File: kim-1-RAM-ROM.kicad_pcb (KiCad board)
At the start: 2 copper layers, 113.5 x 134.6 mm, 42 parts, among them J1 Conn_03x08, J2 Conn_03x06, J3 Conn_02x08_Counter_Clockwise, SW1 Vectors, SW2 SW_DIP_x08, SW3 SW_DIP_x07, SW4 SW_DIP_x01, SW5 SW_DIP_x01, SW6 Image_set, U1 74LS04, U10 SST39SF020, U11 628128, U2 74LS08, U3 74LS08, U4 74HCT541, U5 74HCT541, U6 74LS133, U7 74LS145, U8 74LS145, U9 74LS145, X1 EDGE_CONN

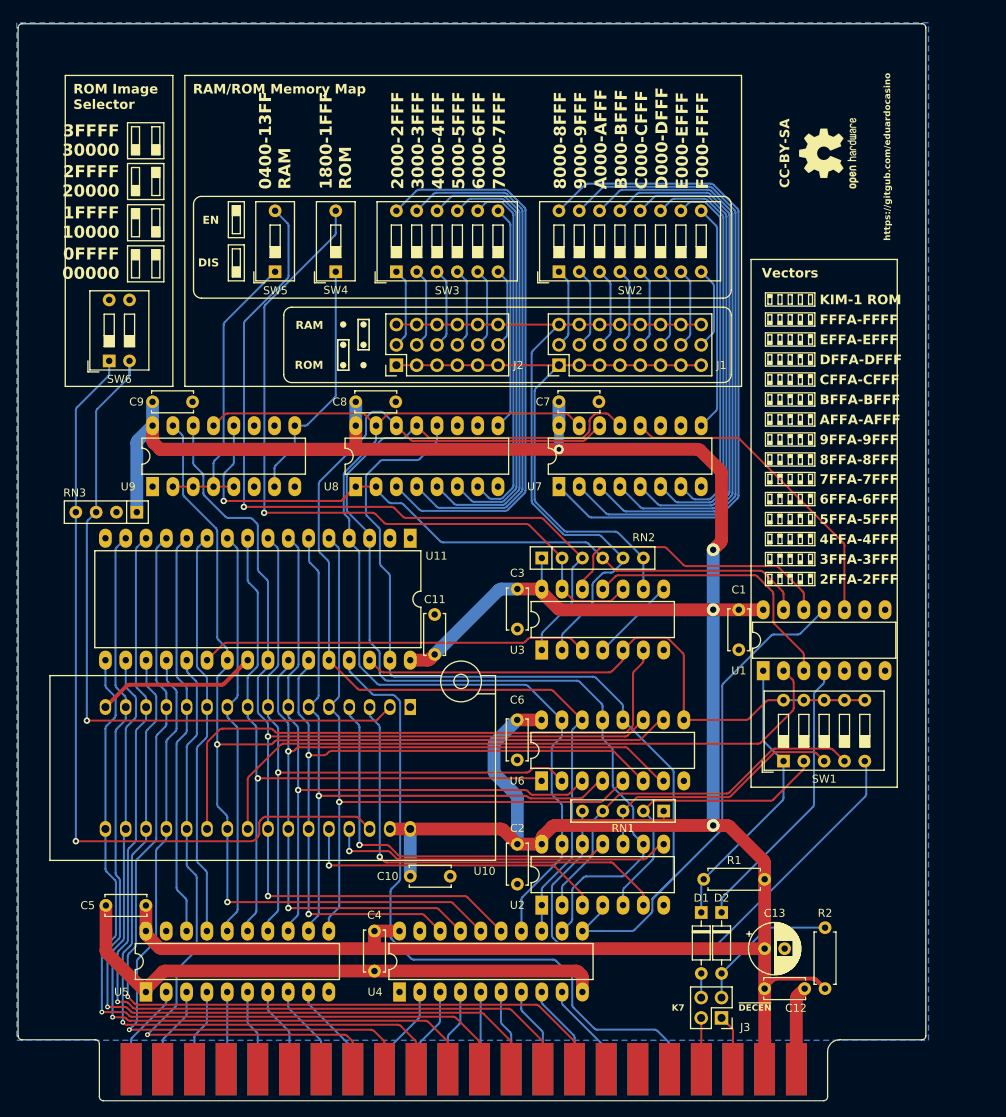
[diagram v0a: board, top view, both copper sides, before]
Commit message: Add option to support the MTU floppy controller boot prom
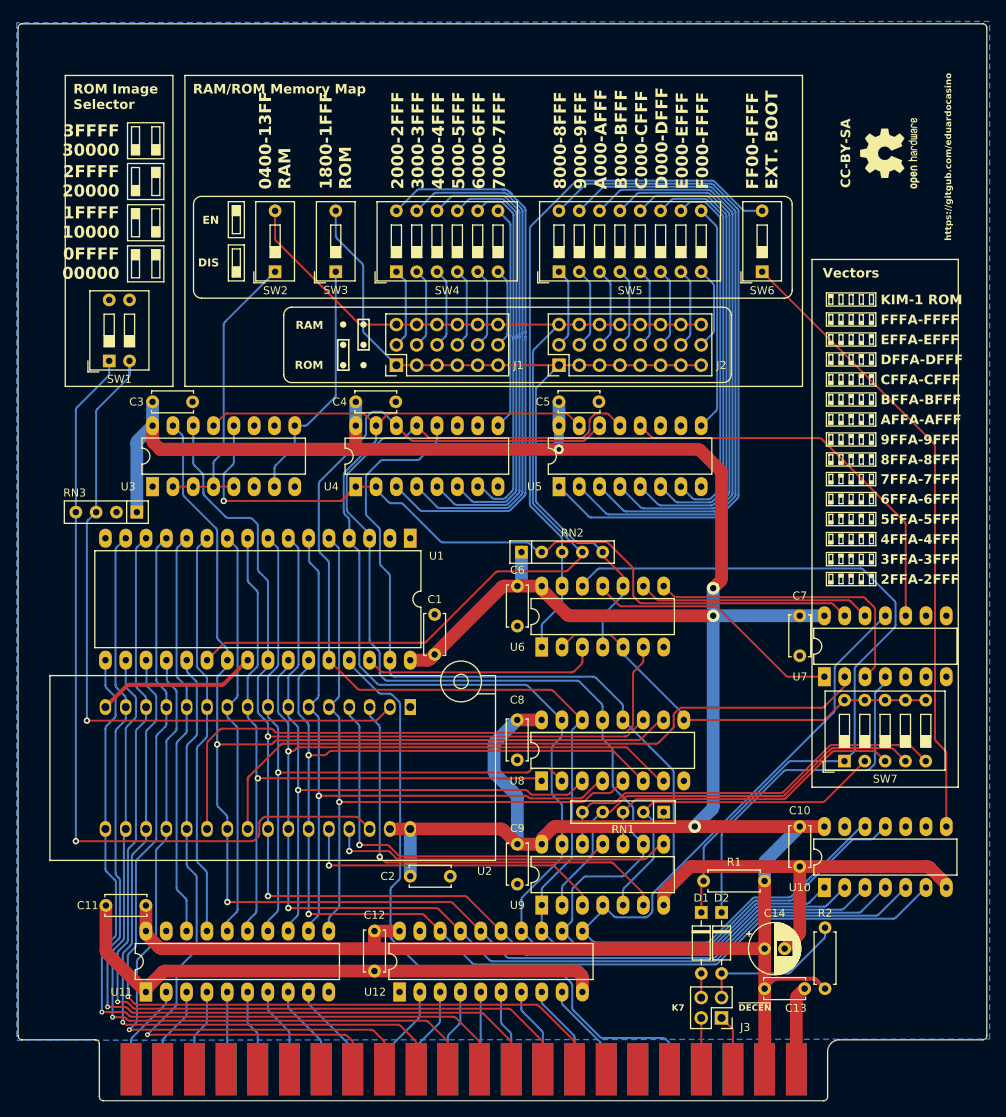
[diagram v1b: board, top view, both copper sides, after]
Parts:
- added C10: 100nF, Capacitor_THT:C_Disc_D5.0mm_W2.5mm_P5.00mm, F.Cu at (149.5, 167.1)
- added SW6: SW_DIP_x01, Button_Switch_THT:SW_DIP_SPSTx01_Slide_9.78x4.72mm_W7.62mm_P2.54mm, F.Cu at (144.8, 97.8)
- added U10: 74LS30, Package_DIP:DIP-14_W7.62mm_LongPads, F.Cu at (152.6, 174.8)
- RN2: footprint Resistor_THT:R_Array_SIP6 -> Resistor_THT:R_Array_SIP5
- moved U7 7.69 mm to (152.6, 148.4)
- moved C7 7.66 mm to (149.5, 140.8)
- moved REF** 7.62 mm to (160.7, 83.0)
- moved SW7 7.62 mm to (155.1, 158.9)
- moved RN2 2.65 mm to (114.7, 132.8)
- moved C6 0.37 mm to (114.2, 137.1)
- moved U6 0.37 mm to (117.2, 144.7)
- moved R1 0.21 mm to (137.4, 173.9)
- moved RN1 0.13 mm to (132.5, 165.3)
- renumbered C11 to C1, C5 to C11, C4 to C12, C12 to C13, C13 to C14, C10 to C2, C9 to C3, C8 to C4, C7 to C5, C3 to C6, C1 to C7, C6 to C8, C2 to C9, J2 to J1, J1 to J2, SW6 to SW1, SW5 to SW2, SW4 to SW3, SW3 to SW4, SW2 to SW5, SW1 to SW7, U11 to U1, U5 to U11, U4 to U12, U10 to U2, U9 to U3, U8 to U4, U7 to U5, U3 to U6, U1 to U7, U6 to U8, U2 to U9
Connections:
- RN2 pad 4: Net-(RN2-R3) -> Net-(J1-Pin_12)
- RN2 pad 5: Net-(J1-Pin_12) -> Net-(J1-Pin_1)
- SW2 pad 2: Net-(RN2-R2) -> Net-(J1-Pin_12)
- SW3 pad 2: Net-(RN2-R1) -> Net-(J1-Pin_1)
- SW7 pad 10: Net-(U11-CS2) -> Net-(SW7-Pad10)
- SW7 pad 6: Net-(U11-CS2) -> Net-(SW7-Pad10)
- SW7 pad 7: Net-(U11-CS2) -> Net-(SW7-Pad10)
- SW7 pad 8: Net-(U11-CS2) -> Net-(SW7-Pad10)
- SW7 pad 9: Net-(U11-CS2) -> Net-(SW7-Pad10)
- U1 pad 22: Net-(U11-~{CS1}) -> Net-(J1-Pin_12)
- U1 pad 30: Net-(U11-CS2) -> Net-(U1-CS2)
- U3 pad 12: Net-(RN2-R3) -> Net-(RN2-R1)
- U4 pad 1: Net-(RN2-R3) -> Net-(RN2-R1)
- U4 pad 2: Net-(RN2-R3) -> Net-(RN2-R1)
- U6 pad 10: Net-(RN2-R1) -> Net-(J1-Pin_1)
- U6 pad 11: Net-(U1-Pad3) -> Net-(U6-Pad11)
- U6 pad 12: Net-(U1-Pad12) -> Net-(D1-K)
- U6 pad 13: Net-(RN2-R1) -> Net-(RN2-R2)
- U6 pad 2: Net-(J1-Pin_12) -> Net-(SW7-Pad10)
- U6 pad 3: Net-(U11-~{CS1}) -> Net-(U1-CS2)
- U6 pad 4: Net-(U3-Pad4) -> Net-(J1-Pin_1)
- U6 pad 5: Net-(U11-CS2) -> Net-(SW7-Pad10)
- U6 pad 8: Net-(U3-Pad4) -> Net-(U6-Pad8)
- U6 pad 9: Net-(J1-Pin_1) -> Net-(U6-Pad9)
- U7 pad 1: Net-(D1-K) -> Net-(U6-Pad11)
- U7 pad 12: Net-(U1-Pad12) -> Net-(U6-Pad9)
- U7 pad 13: Net-(RN2-R3) -> Net-(RN2-R1)
- U7 pad 3: Net-(U1-Pad3) -> Net-(U6-Pad8)
- U8 pad 9: Net-(U11-CS2) -> Net-(SW7-Pad10)
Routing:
- net Net-(RN2-R3): track 90.8 -> 0.00 mm, vias 1 -> 0
- net Net-(SW6-Pad1): track 0.00 -> 78.8 mm
- net Net-(U11-CS2): track 75.0 -> 0.00 mm
- net /A8: track 93.7 -> 160.1 mm
- net /A9: track 103.6 -> 164.6 mm
- net Net-(D1-K): track 35.8 -> 94.9 mm
- net /A10: track 153.3 -> 208.9 mm
- net Net-(J1-Pin_12): track 91.2 -> 146.3 mm
- net Net-(SW7-Pad10): track 0.00 -> 52.3 mm
- net GND: track 101.5 -> 152.0 mm
- net /A11: track 143.9 -> 194.0 mm
- net Net-(U11-~{CS1}): track 48.6 -> 0.00 mm
- net /A14: track 133.0 -> 180.2 mm
- net /A12: track 138.0 -> 182.7 mm
- net /A13: track 128.0 -> 167.3 mm
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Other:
- board size 113.5 x 134.6 mm -> 121.1 x 134.6 mm
- board text added: "FF00-FFFF EXT. BOOT"

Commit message: Minor silkscreen changes
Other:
- board text added: "1"
- board text added: "22"
- board text added: "A"
- board text added: "Z"
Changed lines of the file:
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@@
   (gr_line (start 154.45 193.78) (end 172.35 193.78)
     (stroke (width 0.1) (type default)) (layer "Edge.Cuts"))
+  (gr_text "Z" (at 151.04 193.3) (layer "B.SilkS")
+    (effects (font (size 1 1) (thickness 0.15)) (justify right bottom mirror))
+  )
+  (gr_text "A" (at 63.88 193.3) (layer "B.SilkS")
+    (effects (font (size 1 1) (thickness 0.15)) (justify left bottom mirror))
+  )
   (gr_text "F000-FFFF" (at 138.19 87.48 90) (layer "F.SilkS")
     (effects (font (face "Consolas") (size 1.5 1.5) (thickness 0.3) bold) (justify left bottom))
@@
     )
   )
+  (gr_text "1" (at 63.88 193.3) (layer "F.SilkS")
+    (effects (font (size 1 1) (thickness 0.15)) (justify right bottom))
+  )
   (gr_text "8FFA-8FFF" (at 159.57 121.28) (layer "F.SilkS")
     (effects (font (face "Consolas") (size 1.2 1.2) (thickness 0.2) bold) (justify left))
@@
     )
   )
+  (gr_text "22" (at 151.04 193.3) (layer "F.SilkS")
+    (effects (font (size 1 1) (thickness 0.15)) (justify left bottom))
+  )
   (gr_text "1800-1FFF\nROM" (at 91.47 87.48 90) (layer "F.SilkS")

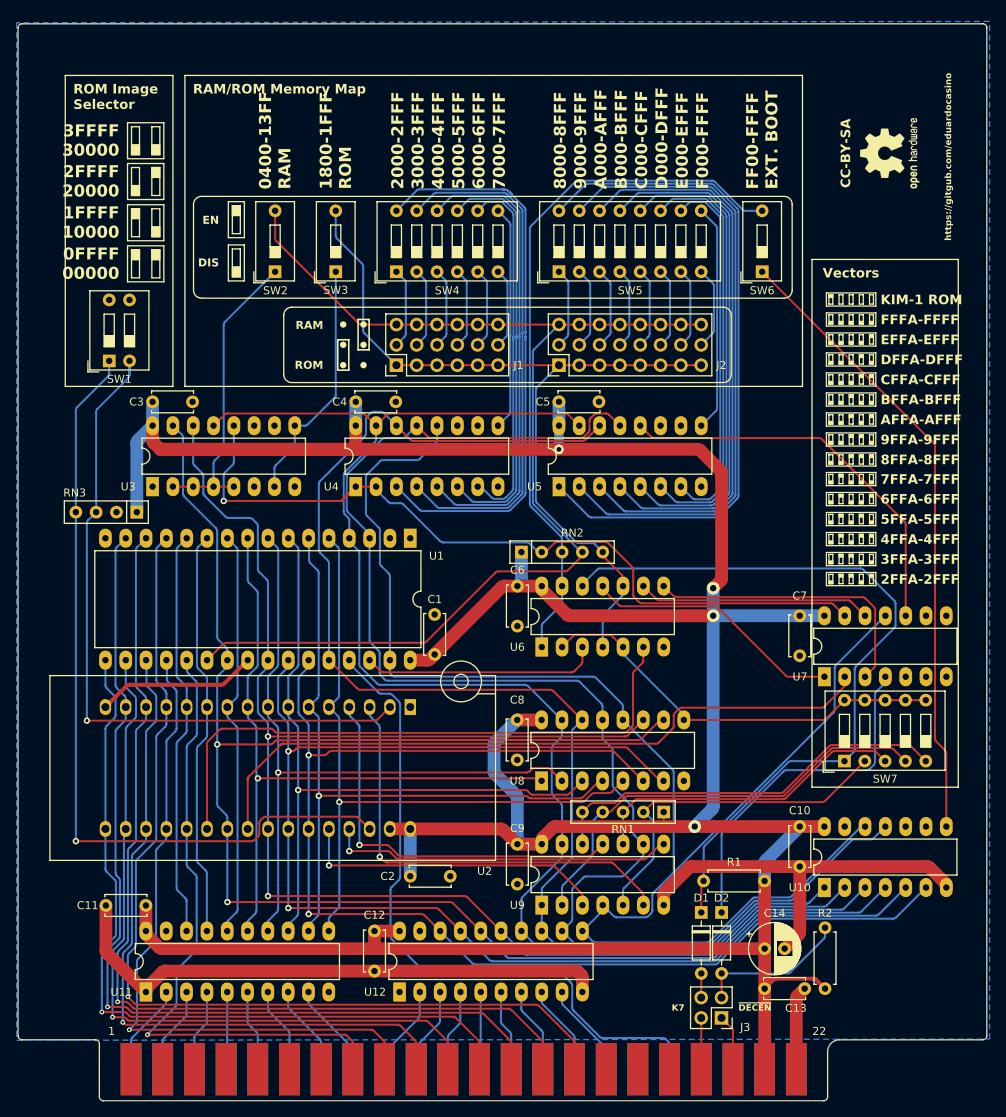
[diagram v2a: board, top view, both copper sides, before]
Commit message: Remove useless switch and simplify design
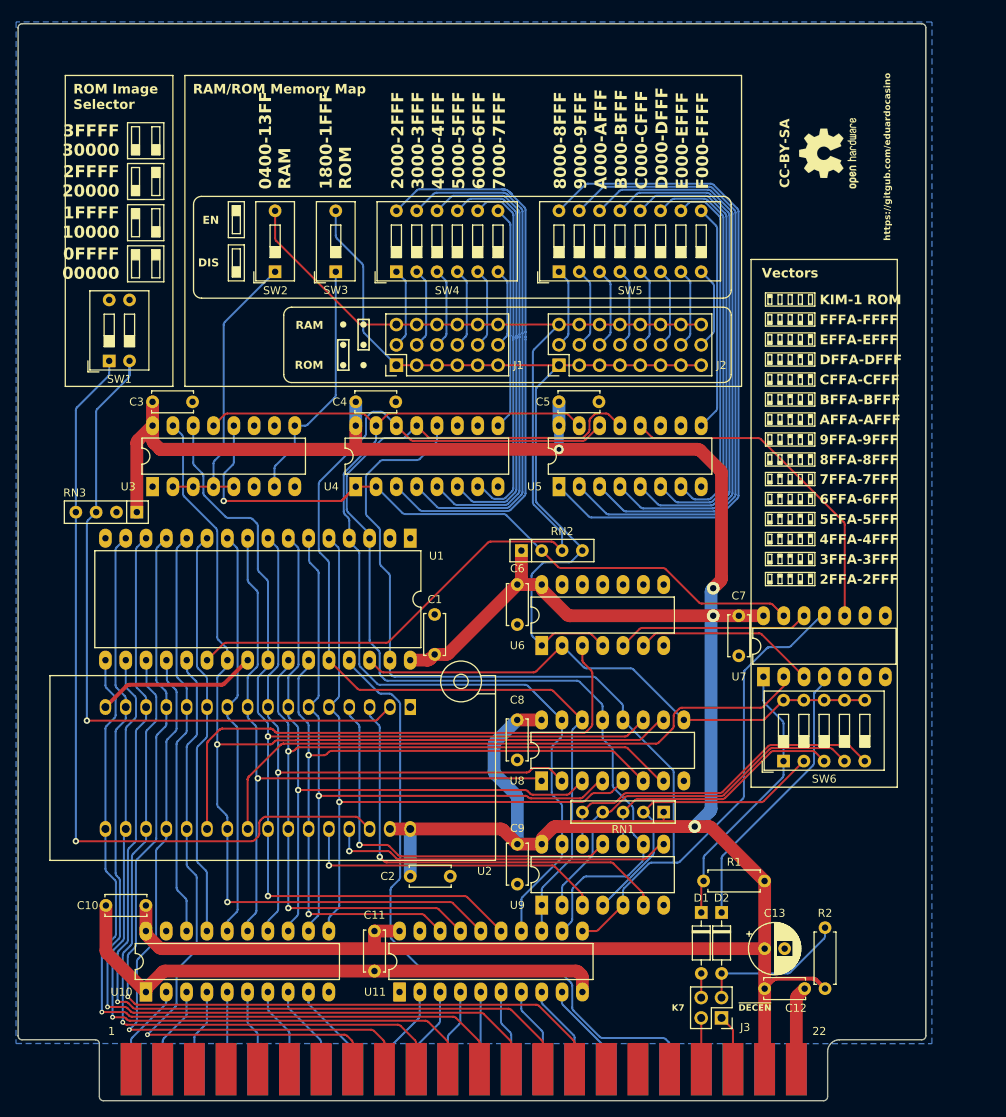
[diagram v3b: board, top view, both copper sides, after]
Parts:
- removed the C10 at (149.5, 167.1)
- removed the SW6 at (144.8, 97.8)
- removed the U10 at (152.6, 174.8)
- RN2: footprint Resistor_THT:R_Array_SIP5 -> Resistor_THT:R_Array_SIP4
- moved C7 7.62 mm to (141.8, 140.8)
- moved REF** 7.62 mm to (153.1, 83.0)
- moved SW6 7.62 mm to (147.4, 158.9)
- moved U7 7.62 mm to (144.9, 148.4)
- moved C6 0.19 mm to (114.2, 136.9)
- moved RN2 0.19 mm to (114.7, 132.6)
- moved U6 0.19 mm to (117.2, 144.5)
- renumbered C11 to C10, C12 to C11, C13 to C12, C14 to C13, SW7 to SW6, U11 to U10, U12 to U11
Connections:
- RN2 pad 3: Net-(RN2-R2) -> Net-(J1-Pin_12)
- RN2 pad 4: Net-(J1-Pin_12) -> Net-(J1-Pin_1)
- SW6 pad 10: Net-(SW7-Pad10) -> Net-(U1-CS2)
- SW6 pad 6: Net-(SW7-Pad10) -> Net-(U1-CS2)
- SW6 pad 7: Net-(SW7-Pad10) -> Net-(U1-CS2)
- SW6 pad 8: Net-(SW7-Pad10) -> Net-(U1-CS2)
- SW6 pad 9: Net-(SW7-Pad10) -> Net-(U1-CS2)
- U6 pad 1: Net-(RN2-R2) -> Net-(J1-Pin_1)
- U6 pad 10: Net-(J1-Pin_1) -> GND
- U6 pad 11: Net-(U6-Pad11) -> unconnected-(U6-Pad11)
- U6 pad 12: Net-(D1-K) -> GND
- U6 pad 13: Net-(RN2-R2) -> GND
- U6 pad 2: Net-(SW7-Pad10) -> Net-(U1-CS2)
- U6 pad 3: Net-(U1-CS2) -> Net-(U2-CE)
- U6 pad 5: Net-(SW7-Pad10) -> Net-(U6-Pad5)
- U6 pad 6: Net-(U2-CE) -> Net-(U6-Pad6)
- U6 pad 8: Net-(U6-Pad8) -> unconnected-(U6-Pad8)
- U6 pad 9: Net-(U6-Pad9) -> GND
- U7 pad 1: Net-(U6-Pad11) -> Net-(D1-K)
- U7 pad 12: Net-(U6-Pad9) -> Net-(U6-Pad5)
- U7 pad 3: Net-(U6-Pad8) -> Net-(U6-Pad6)
- U8 pad 9: Net-(SW7-Pad10) -> Net-(U1-CS2)
- U9 pad 4: /A15 -> Net-(RN1-R1)
- U9 pad 5: Net-(RN1-R1) -> /A15
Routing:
- net Net-(RN2-R2): track 88.0 -> 0.00 mm
- net Net-(SW6-Pad1): track 78.8 -> 0.00 mm
- net /A8: track 160.1 -> 93.7 mm
- net /A9: track 164.6 -> 103.6 mm
- net Net-(D1-K): track 94.9 -> 34.9 mm
- net /A10: track 208.9 -> 153.3 mm
- net Net-(SW7-Pad10): track 52.3 -> 0.00 mm
- net GND: track 152.0 -> 101.5 mm
- net /A11: track 194.0 -> 143.9 mm
- net /A14: track 180.2 -> 133.3 mm
- net /A15: track 194.8 -> 148.2 mm
- net /A12: track 182.7 -> 138.0 mm
- net /A13: track 167.3 -> 128.0 mm
- net Net-(U1-CS2): track 29.7 -> 68.7 mm
- net Net-(U6-Pad8): track 36.6 -> 0.00 mm
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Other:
- board size 121.1 x 134.6 mm -> 113.5 x 134.6 mm
- board text removed: "FF00-FFFF EXT. BOOT"

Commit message: Release 2.0. Fixes issue #1
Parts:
- removed the SW3 at (91.5, 97.8)
- RN2: value 3k3 -> 3K3
- SW2: value SW_DIP_x01 -> SW_DIP_x03; footprint Button_Switch_THT:SW_DIP_SPSTx01_Slide_9.78x4.72mm_W7.62mm_P2.54mm -> Button_Switch_THT:SW_DIP_SPSTx03_Slide_9.78x9.8mm_W7.62mm_P2.54mm
- moved U6 4.52 mm to (117.2, 140.0)
- moved C6 4.52 mm to (114.2, 132.4)
- moved RN2 3.40 mm to (114.7, 129.2)
- moved REF** 2.50 mm to (153.1, 80.5)
- moved SW2 2.46 mm to (86.3, 97.8)
- turned C7 to 180 degrees
- renumbered SW4 to SW3, SW5 to SW4, SW6 to SW5
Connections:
- SW2 pad 1: Net-(U3-Q1) -> Net-(U3-Q0)
- SW2 pad 2: Net-(J1-Pin_12) -> Net-(U3-Q1)
- U3 pad 1: unconnected-(U3-Q0-Pad1) -> Net-(U3-Q0)
- U6 pad 11: unconnected-(U6-Pad11) -> Net-(U6-Pad11)
- U6 pad 12: GND -> Net-(J1-Pin_1)
- U6 pad 13: GND -> Net-(J1-Pin_12)
- U6 pad 4: Net-(J1-Pin_1) -> Net-(U6-Pad11)
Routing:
- net Net-(U3-Q0): track 0.00 -> 36.9 mm
- net Net-(J1-Pin_1): track 113.2 -> 97.6 mm
- net +5V: track 424.3 -> 433.1 mm, vias 4 -> 3
- net Net-(U6-Pad11): track 0.00 -> 7.62 mm
- net Net-(U1-CS2): track 68.7 -> 73.5 mm
- net Net-(U2-CE): track 70.8 -> 75.2 mm
- net Net-(U3-Q1): track 37.6 -> 39.7 mm
- net Net-(U6-Pad5): track 24.1 -> 25.4 mm
- net Net-(U6-Pad6): track 22.9 -> 23.5 mm
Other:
- board text added: "0400-13FF"
- board text added: "1FFA-1FFF"
- board text added: "PCB Revision 2.0"
- board text added: "SYSTM RAM"
- board text added: "SYSTM ROM"
- board text removed: "0400-13FF RAM"
- board text removed: "1800-1FFF ROM"
